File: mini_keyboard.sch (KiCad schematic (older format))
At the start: 2 parts, among them SW1 SW_DIP_x01, U1 ARDUINO_MICRO_SHIELD

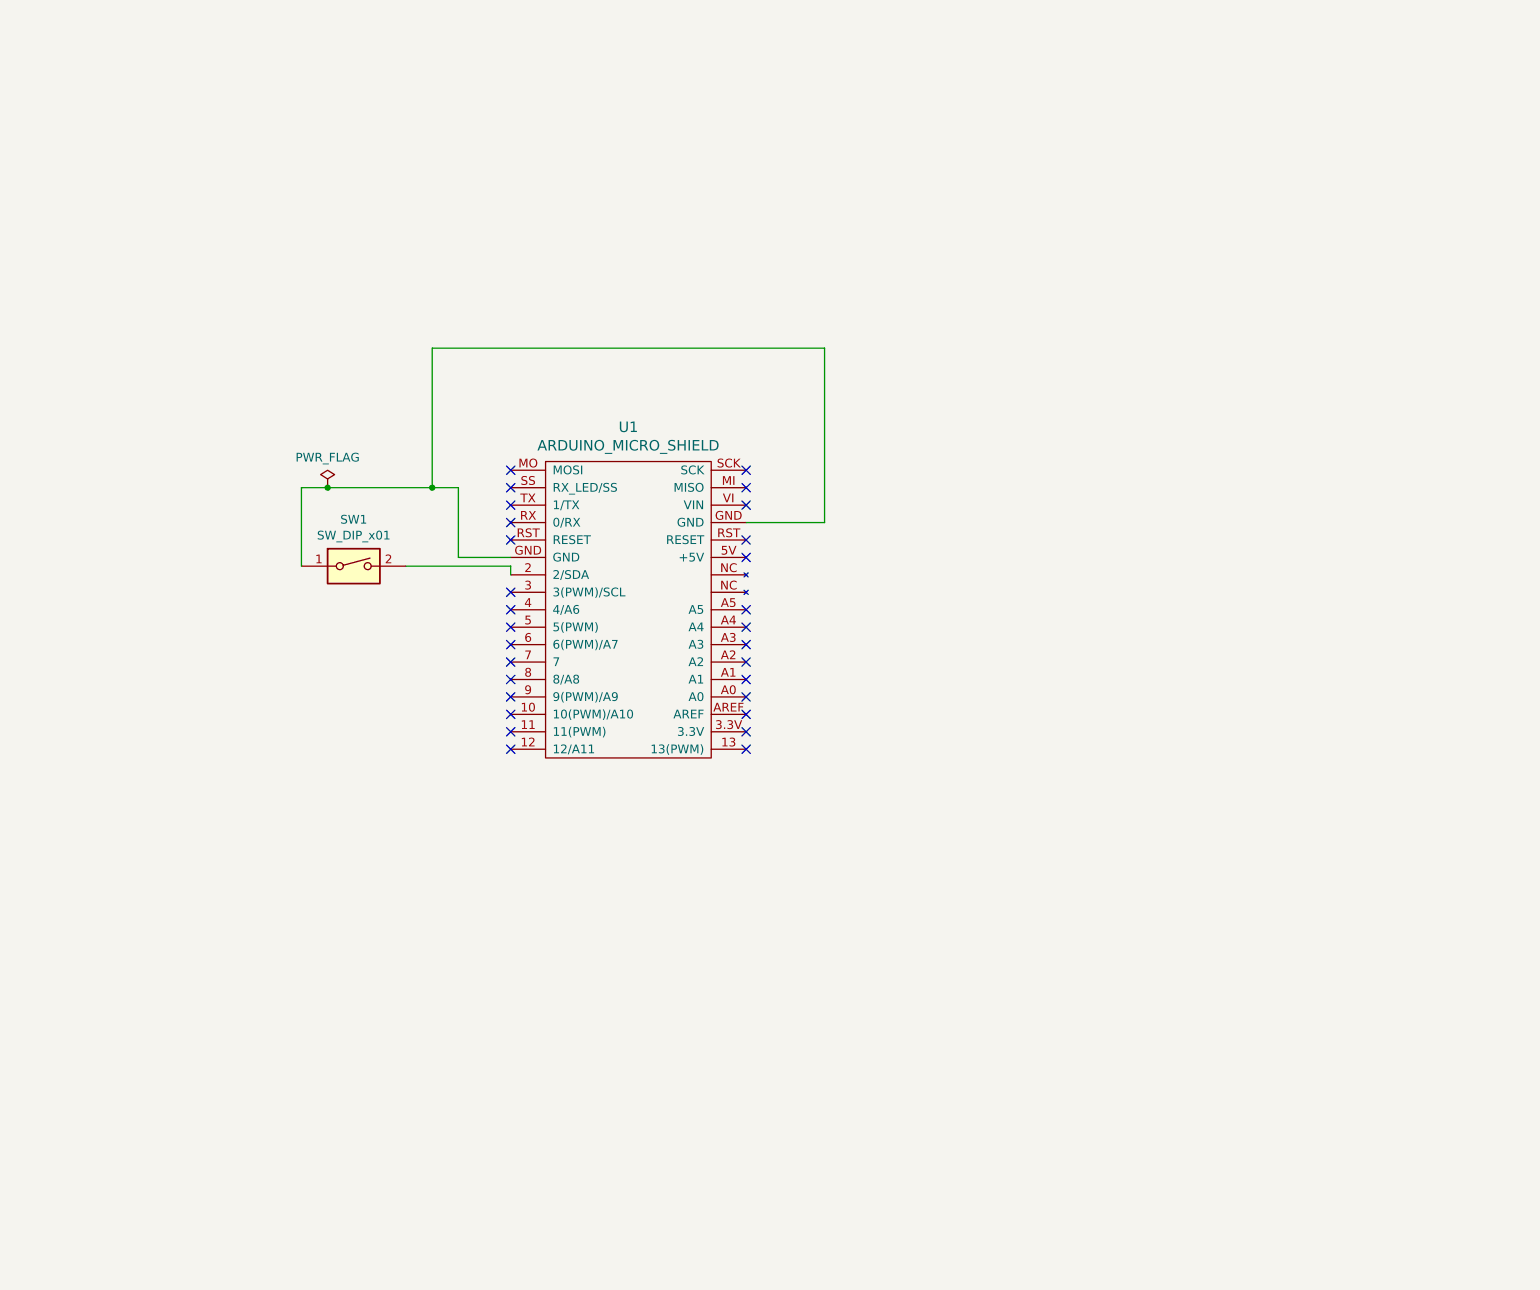
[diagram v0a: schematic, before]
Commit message: Added all components
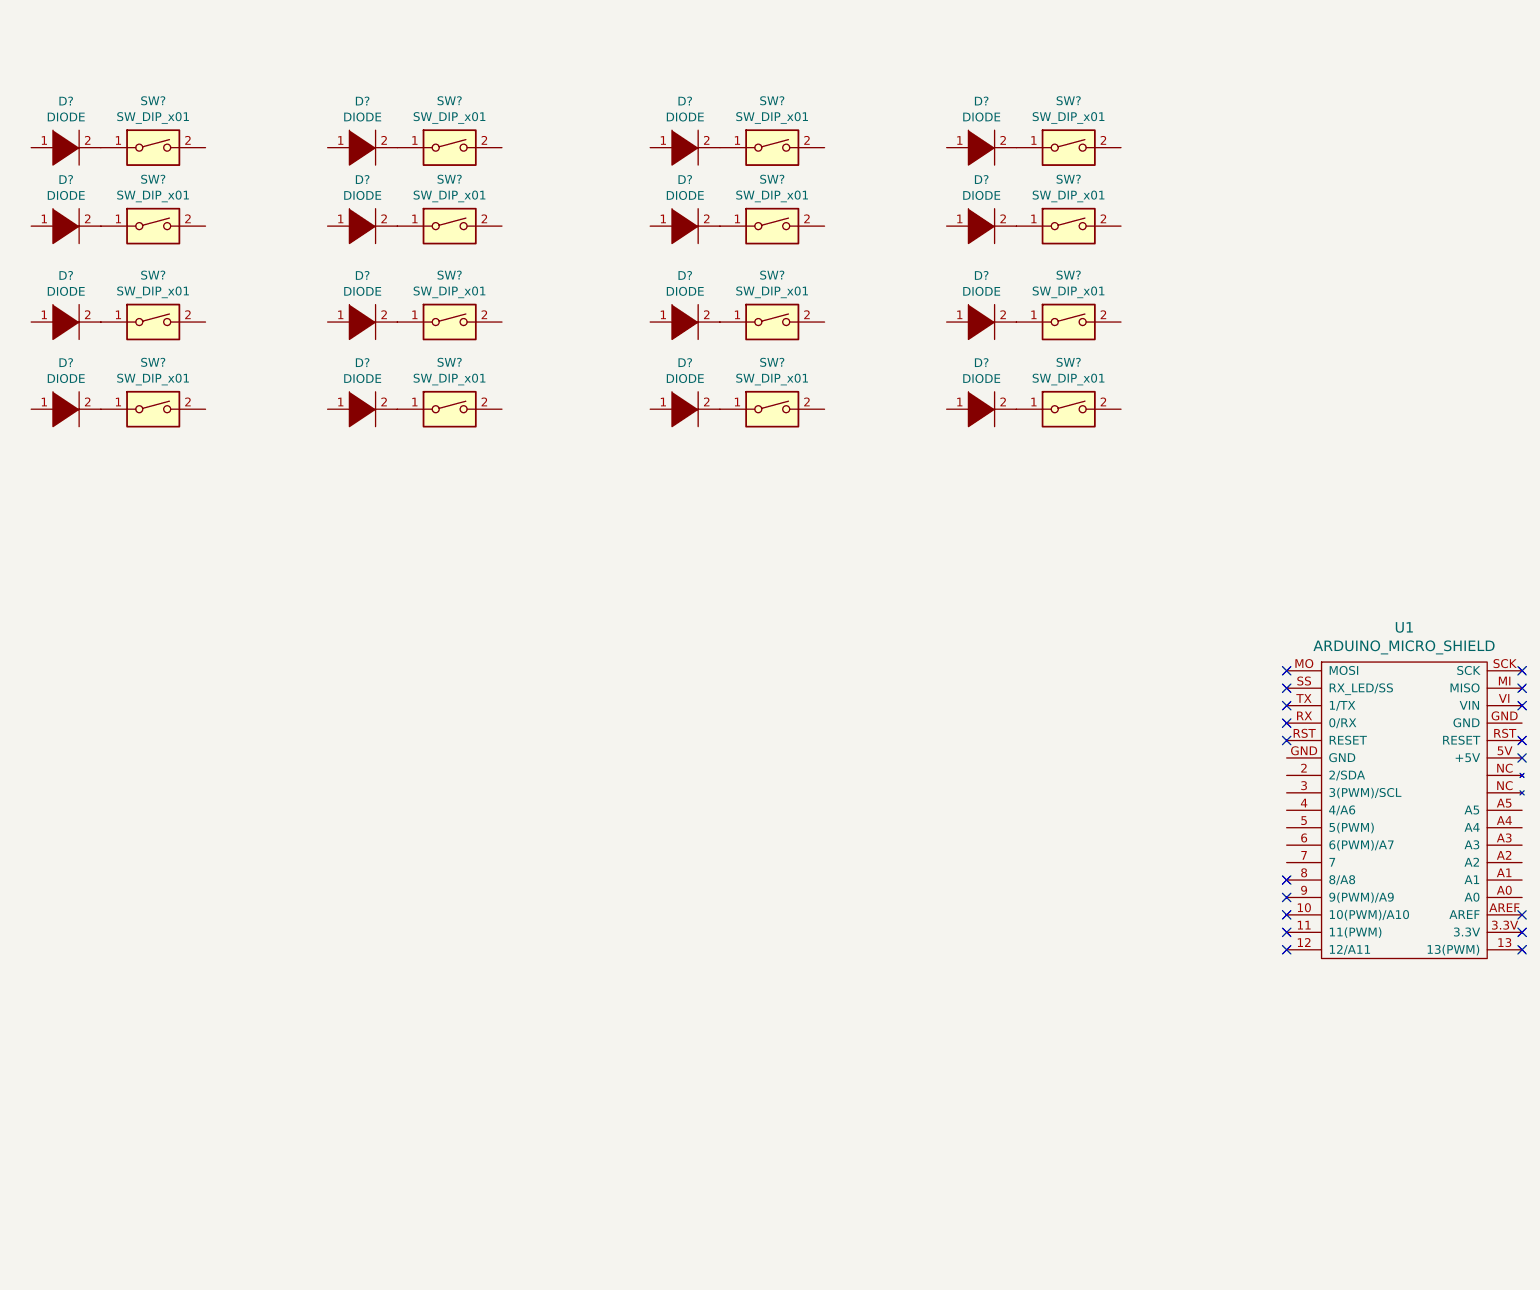
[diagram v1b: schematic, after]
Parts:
- removed SW1: SW_DIP_x01, Button_Switch_Keyboard:SW_Cherry_MX_1.00u_Plate, symbol Switch:SW_DIP_x01
- added D? (x16): DIODE, symbol pspice:DIODE
- added SW? (x16): SW_DIP_x01, Button_Switch_Keyboard:SW_Cherry_MX_1.00u_Plate, symbol Switch:SW_DIP_x01
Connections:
- new net: D?.2 (A), SW?.1 (x16)
- no-connect marks 29 -> 18
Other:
- moved on the sheet: U1

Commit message: Added 16 buttons, need 4 more
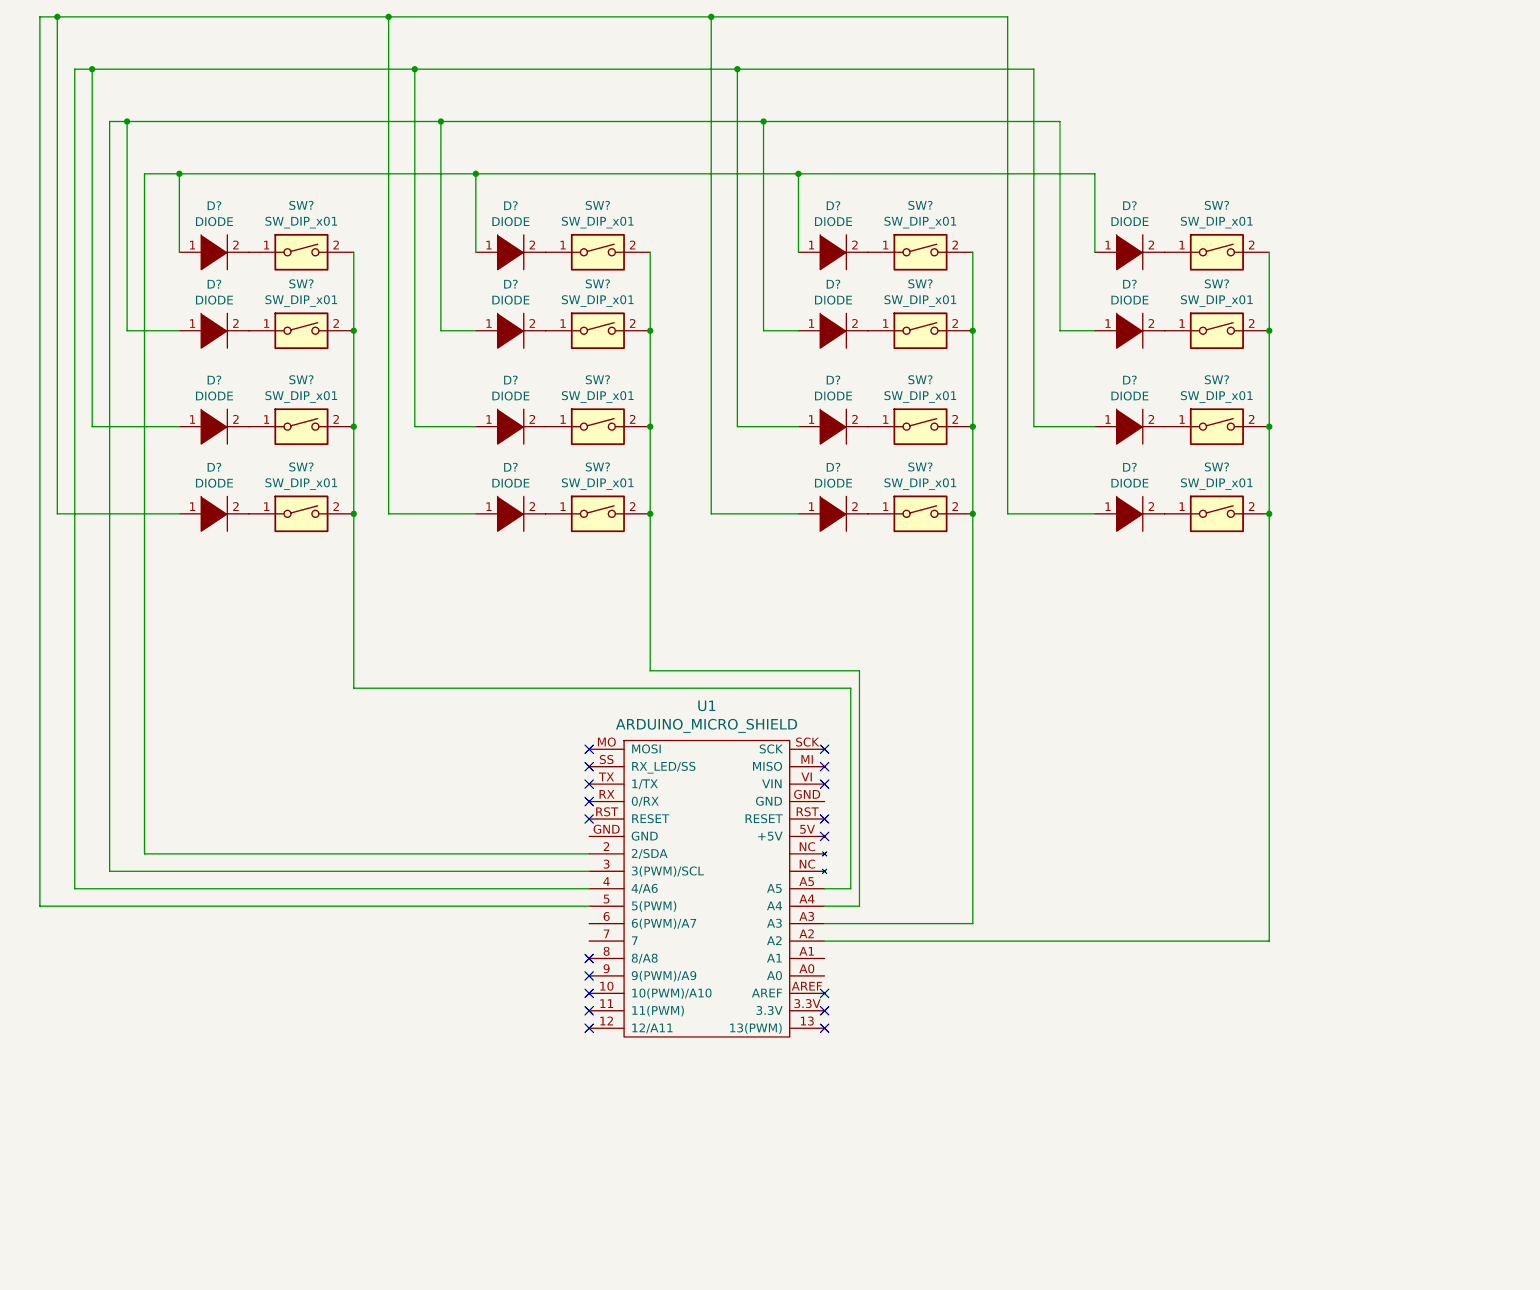
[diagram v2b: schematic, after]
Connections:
- net at U1.2 (2/SDA): now also D?.1 (K), D?.1 (K), D?.1 (K), D?.1 (K)
- net at U1.3 (3(PWM)/SCL): now also D?.1 (K), D?.1 (K), D?.1 (K), D?.1 (K)
- net at U1.4 (4/A6): now also D?.1 (K), D?.1 (K), D?.1 (K), D?.1 (K)
- net at U1.5 (5(PWM)): now also D?.1 (K), D?.1 (K), D?.1 (K), D?.1 (K)
- net at U1.A2: now also SW?.2, SW?.2, SW?.2, SW?.2
- net at U1.A3: now also SW?.2, SW?.2, SW?.2, SW?.2
- net at U1.A4: now also SW?.2, SW?.2, SW?.2, SW?.2
- net at U1.A5: now also SW?.2, SW?.2, SW?.2, SW?.2
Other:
- moved on the sheet: D?, SW?, U1

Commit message: added 20 buttons
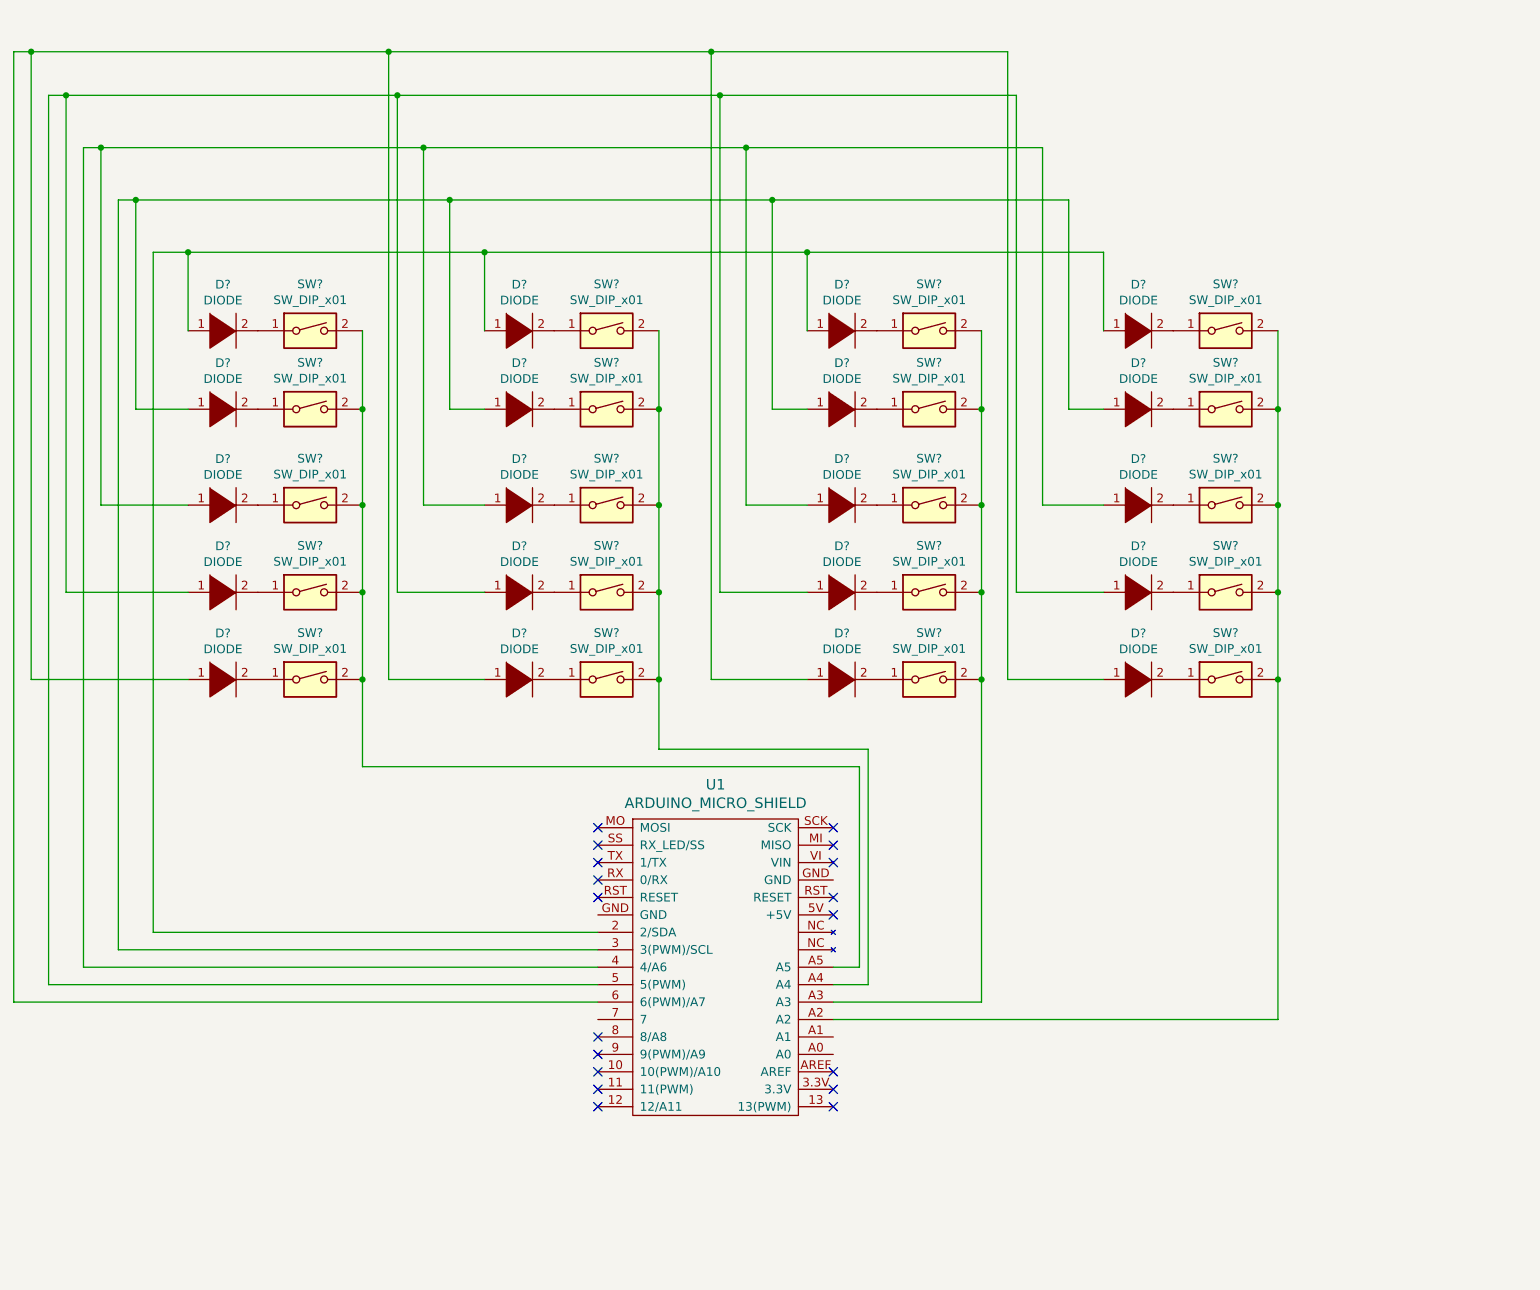
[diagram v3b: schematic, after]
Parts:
- added D? (x4): DIODE, symbol pspice:DIODE
- added SW? (x4): SW_DIP_x01, Button_Switch_Keyboard:SW_Cherry_MX_1.00u_Plate, symbol Switch:SW_DIP_x01
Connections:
- net at U1.6 (6(PWM)/A7): now also D?.1 (K), D?.1 (K), D?.1 (K), D?.1 (K)
- net at SW?.2, SW?.2, SW?.2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: now also SW?.2 (x4)
- new net: D?.2 (A), SW?.1 (x4)
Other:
- moved on the sheet: D?, SW?, U1

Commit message: added joystick
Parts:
- added U?: Joystick, symbol joystick:Joystick
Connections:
- wire segments 94 -> 109
- no-connect marks 18 -> 17
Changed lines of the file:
@@
 NoConn ~ 6350 6600
 NoConn ~ 6350 6500
-NoConn ~ 6350 5600
 NoConn ~ 6350 5500
 NoConn ~ 6350 5300
@@
 Wire Wire Line
 	1750 650  3800 650
+Wire Wire Line
+	6350 5600 7550 5600
+Wire Wire Line
+	7550 5600 7550 5750
+Wire Wire Line
+	6350 5400 7750 5400
+Wire Wire Line
+	7400 5850 7400 6300
+Wire Wire Line
+	7400 6300 6350 6300
+Wire Wire Line
+	6350 6400 7500 6400
+Wire Wire Line
+	7500 6400 7500 5950
+Wire Wire Line
+	7750 6900 4750 6900
+Wire Wire Line
+	4750 6900 4750 6200
+Wire Wire Line
+	4750 6200 5000 6200
+Wire Wire Line
+	7750 5850 7400 5850
+Wire Wire Line
+	7500 5950 7750 5950
+Wire Wire Line
+	7750 6050 7750 6900
+Wire Wire Line
+	7750 5400 7750 5650
+Wire Wire Line
+	7550 5750 7750 5750
+$Comp
+L joystick:Joystick U?
+U 1 1 5FD914AC
+P 8100 5900
+F 0 "U?" H 8428 5971 50  0000 L CNN
+F 1 "Joystick" H 8428 5880 50  0000 L CNN
+F 2 "" H 8100 5900 50  0001 C CNN
+F 3 "" H 8100 5900 50  0001 C CNN
+	1    8100 5900
+	1    0    0    -1
+$EndComp
 $EndSCHEMATC

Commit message: Mad joystick footprint, getting errors in lib editor
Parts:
- gave numbers to parts that had none: 41
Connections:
- no-connect marks 17 -> 18

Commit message: PCB ready, no cables
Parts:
- D1, D10, D11, D12, D13, D14, D15, D16, D17, D18, D19, D2, D20, D3, D4, D5, D6, D7, D8, D9: footprint (none) -> Diode_THT:D_T-1_P5.08mm_Horizontal
- U2: footprint (none) -> Joystick:Joystick; symbol joystick:Joystick -> mini_keyboard-rescue:Joystick-joystick
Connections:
- wire segments 109 -> 111
